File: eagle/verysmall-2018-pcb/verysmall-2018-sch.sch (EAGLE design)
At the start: 3 parts, among them IC1 7805, U1 ESP-WROOM-32, U2 AMS1117-3.3

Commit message: falta conferir pinagem ponte h
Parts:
- added C1: 100nF, rcl:C-EU075-032X103
- added C2: 33uF, rcl:CPOL-USE2-5
- added R1: 10M, rcl:R-EU_0204/7
- added R2: 2.4M, rcl:R-EU_0204/7
- added R3: 1M, rcl:R-EU_0204/7
- added SV1: R, con-lstb:MA08-1
- added SV2: L, con-lstb:MA08-1
- added U$1: MP1584, MP1584-dc-brick:MP1584
- added U3: GY-521MPU6050, gy-521:GY-521MPU6050
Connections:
- net N$1 renamed 3.3V
- new net 5V: C2.+, IC1.OUT, U2.VIN, U3.VCC
- new net A01: SV2.4
- new net A02: SV2.5
- new net AI1: SV1.6
- new net AI2: SV1.7
- new net B01: SV2.7
- new net B02: SV2.6
- new net BAT_VCC: C1.2, IC1.IN, R1.1, U$1.VIN+
- new net BI1: SV1.4
- new net BI2: SV1.3
- new net N$1: U1.IO4, U3.SCL
- new net N$2: R2.1, R3.2
- new net N$3: U1.IO5, U3.SDA
- new net N$4: U1.IO14, U3.INT
- new net PWMA: SV1.8
- new net PWMB: SV1.2
- new net STBY: SV1.5
- new net VCC: SV2.2
- new net VM: SV2.1, U$1.VOUT+
- new net V_OUT: R1.2, R2.2, U1.SENSOR_VP
- net GND: now also C1.1, C2.-, R3.1, SV1.1, SV2.3, SV2.8, U$1.VIN-, U$1.VOUT-, U1.GND, U3.GND
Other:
- note added: "Circuito nivel logico 3.3V"
- note added: "Circuito nivel logico 5V"
- note added: "Divisor tensao para leitura da bateria"
- note added: "Stepdown Motores"
- note added: "ponte h"
- moved on the sheet: IC1, U1, U2

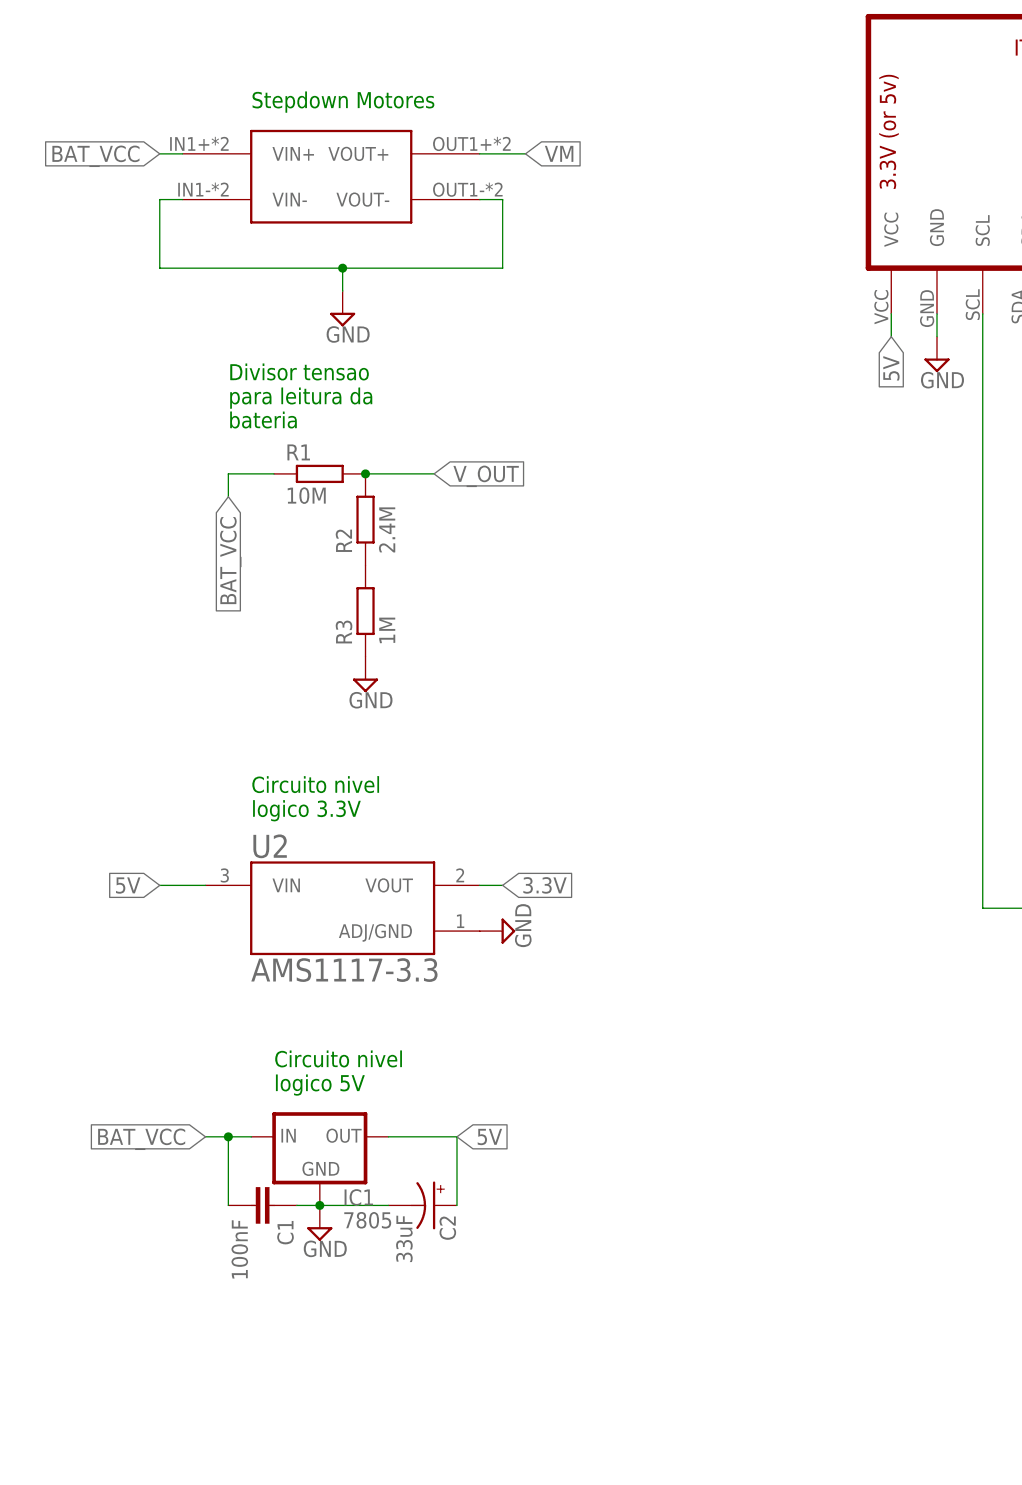
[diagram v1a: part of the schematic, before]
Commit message: falta conferir pinagem ponte h adicao led
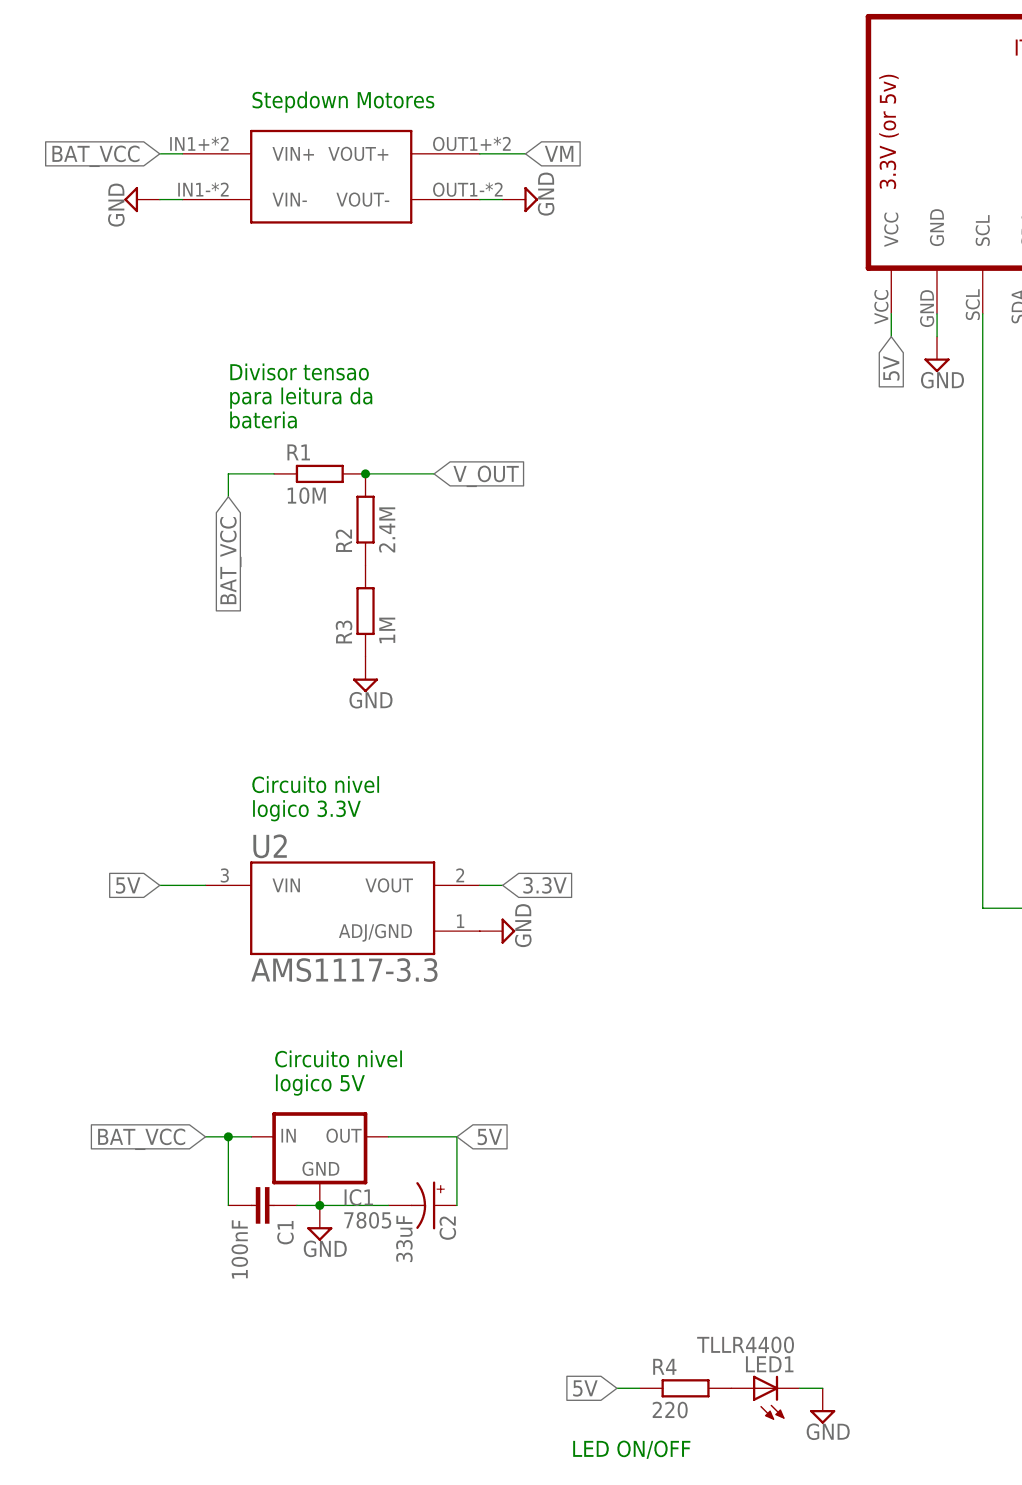
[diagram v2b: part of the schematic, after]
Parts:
- added LED1: TLLR4400, led:TLLR4400
- added R4: 220, rcl:R-EU_0207/7
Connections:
- new net N$5: LED1.A, R4.2
- net 5V: now also R4.1
- net GND: now also LED1.C
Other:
- note added: "LED ON/OFF"
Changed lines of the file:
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@@
 <part name="SUPPLY5" library="supply2" library_urn="urn:adsk.eagle:library:372" deviceset="GND" device=""/>
 <part name="U$1" library="MP1584-dc-brick" deviceset="MP1584" device=""/>
-<part name="SUPPLY6" library="supply2" library_urn="urn:adsk.eagle:library:372" deviceset="GND" device=""/>
 <part name="SV1" library="con-lstb" library_urn="urn:adsk.eagle:library:162" deviceset="MA08-1" device="" package3d_urn="urn:adsk.eagle:package:8343/1" value="R"/>
 <part name="SV2" library="con-lstb" library_urn="urn:adsk.eagle:library:162" deviceset="MA08-1" device="" package3d_urn="urn:adsk.eagle:package:8343/1" value="L"/>
@@
 <part name="SUPPLY8" library="supply2" library_urn="urn:adsk.eagle:library:372" deviceset="GND" device=""/>
 <part name="SUPPLY9" library="supply2" library_urn="urn:adsk.eagle:library:372" deviceset="GND" device=""/>
+<part name="SUPPLY6" library="supply2" library_urn="urn:adsk.eagle:library:372" deviceset="GND" device=""/>
+<part name="SUPPLY10" library="supply2" library_urn="urn:adsk.eagle:library:372" deviceset="GND" device=""/>
+<part name="LED1" library="led" library_urn="urn:adsk.eagle:library:259" deviceset="TLLR4400" device="" package3d_urn="urn:adsk.eagle:package:15797/1"/>
+<part name="R4" library="rcl" library_urn="urn:adsk.eagle:library:334" deviceset="R-EU_" device="0207/7" package3d_urn="urn:adsk.eagle:package:23493/1" value="220"/>
+<part name="SUPPLY11" library="supply2" library_urn="urn:adsk.eagle:library:372" deviceset="GND" device=""/>
 </parts>
 <sheets>
@@
 <text x="-111.76" y="144.78" size="1.778" layer="91">Stepdown Motores</text>
 <text x="101.6" y="83.82" size="1.778" layer="91">ponte h</text>
+<text x="-76.2" y="-5.08" size="1.778" layer="91">LED ON/OFF</text>
 </plain>
 <instances>
@@
 <instance part="SUPPLY5" gate="GND" x="-35.56" y="116.84"/>
 <instance part="U$1" gate="G$1" x="-104.14" y="137.16"/>
-<instance part="SUPPLY6" gate="GND" x="-101.6" y="121.92"/>
 <instance part="SV1" gate="1" x="121.92" y="68.58"/>
 <instance part="SV2" gate="1" x="104.14" y="71.12" rot="R180"/>
@@
 <instance part="SUPPLY8" gate="GND" x="83.82" y="60.96" rot="R270"/>
 <instance part="SUPPLY9" gate="GND" x="144.78" y="60.96" rot="R90"/>
+<instance part="SUPPLY6" gate="GND" x="-81.28" y="134.62" rot="R90"/>
+<instance part="SUPPLY10" gate="GND" x="-124.46" y="134.62" rot="R270"/>
+<instance part="LED1" gate="G$1" x="-55.88" y="2.54" rot="R90"/>
+<instance part="R4" gate="G$1" x="-63.5" y="2.54"/>
+<instance part="SUPPLY11" gate="GND" x="-48.26" y="0"/>
 </instances>
 <busses>
@@
 </segment>
 <segment>
-<pinref part="U$1" gate="G$1" pin="VIN-"/>
-<wire x1="-119.38" y1="134.62" x2="-121.92" y2="134.62" width="0.1524" layer="91"/>
-<wire x1="-121.92" y1="134.62" x2="-121.92" y2="127" width="0.1524" layer="91"/>
-<wire x1="-121.92" y1="127" x2="-101.6" y2="127" width="0.1524" layer="91"/>
-<wire x1="-101.6" y1="127" x2="-83.82" y2="127" width="0.1524" layer="91"/>
-<wire x1="-83.82" y1="127" x2="-83.82" y2="134.62" width="0.1524" layer="91"/>
+<pinref part="SUPPLY7" gate="GND" pin="GND"/>
+<pinref part="SV2" gate="1" pin="3"/>
+<wire x1="86.36" y1="73.66" x2="96.52" y2="73.66" width="0.1524" layer="91"/>
+</segment>
+<segment>
+<pinref part="SV2" gate="1" pin="8"/>
+<wire x1="96.52" y1="60.96" x2="86.36" y2="60.96" width="0.1524" layer="91"/>
+<pinref part="SUPPLY8" gate="GND" pin="GND"/>
+</segment>
+<segment>
+<pinref part="SV1" gate="1" pin="1"/>
+<wire x1="129.54" y1="60.96" x2="142.24" y2="60.96" width="0.1524" layer="91"/>
+<pinref part="SUPPLY9" gate="GND" pin="GND"/>
+</segment>
+<segment>
 <pinref part="U$1" gate="G$1" pin="VOUT-"/>
 <wire x1="-83.82" y1="134.62" x2="-86.36" y2="134.62" width="0.1524" layer="91"/>
 <pinref part="SUPPLY6" gate="GND" pin="GND"/>
-<wire x1="-101.6" y1="124.46" x2="-101.6" y2="127" width="0.1524" layer="91"/>
-<junction x="-101.6" y="127"/>
-</segment>
-<segment>
-<pinref part="SUPPLY7" gate="GND" pin="GND"/>
-<pinref part="SV2" gate="1" pin="3"/>
-<wire x1="86.36" y1="73.66" x2="96.52" y2="73.66" width="0.1524" layer="91"/>
-</segment>
-<segment>
-<pinref part="SV2" gate="1" pin="8"/>
-<wire x1="96.52" y1="60.96" x2="86.36" y2="60.96" width="0.1524" layer="91"/>
-<pinref part="SUPPLY8" gate="GND" pin="GND"/>
-</segment>
-<segment>
-<pinref part="SV1" gate="1" pin="1"/>
-<wire x1="129.54" y1="60.96" x2="142.24" y2="60.96" width="0.1524" layer="91"/>
-<pinref part="SUPPLY9" gate="GND" pin="GND"/>
+</segment>
+<segment>
+<pinref part="U$1" gate="G$1" pin="VIN-"/>
+<wire x1="-119.38" y1="134.62" x2="-121.92" y2="134.62" width="0.1524" layer="91"/>
+<pinref part="SUPPLY10" gate="GND" pin="GND"/>
+</segment>
+<segment>
+<pinref part="LED1" gate="G$1" pin="C"/>
+<wire x1="-50.8" y1="2.54" x2="-48.26" y2="2.54" width="0.1524" layer="91"/>
+<pinref part="SUPPLY11" gate="GND" pin="GND"/>
 </segment>
 </net>
@@
 <label x="-40.64" y="119.38" size="1.778" layer="95" rot="R270" xref="yes"/>
 </segment>
+<segment>
+<pinref part="R4" gate="G$1" pin="1"/>
+<wire x1="-68.58" y1="2.54" x2="-71.12" y2="2.54" width="0.1524" layer="91"/>
+<label x="-71.12" y="2.54" size="1.778" layer="95" rot="R180" xref="yes"/>
+</segment>
 </net>
 <net name="N$1" class="0">
@@
 </segment>
 </net>
+<net name="N$5" class="0">
+<segment>
+<pinref part="LED1" gate="G$1" pin="A"/>
+<pinref part="R4" gate="G$1" pin="2"/>
+</segment>
+</net>
